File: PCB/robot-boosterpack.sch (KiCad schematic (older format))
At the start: 50 parts, among them IC1 DRV8833, IC2 TPS77033, IC3 TPS77050, IC4 LM61428, J1 3.3V Jumper, J2 5V Jumper, J3 9V Jumper, M1 MOTOR, M2 MOTOR

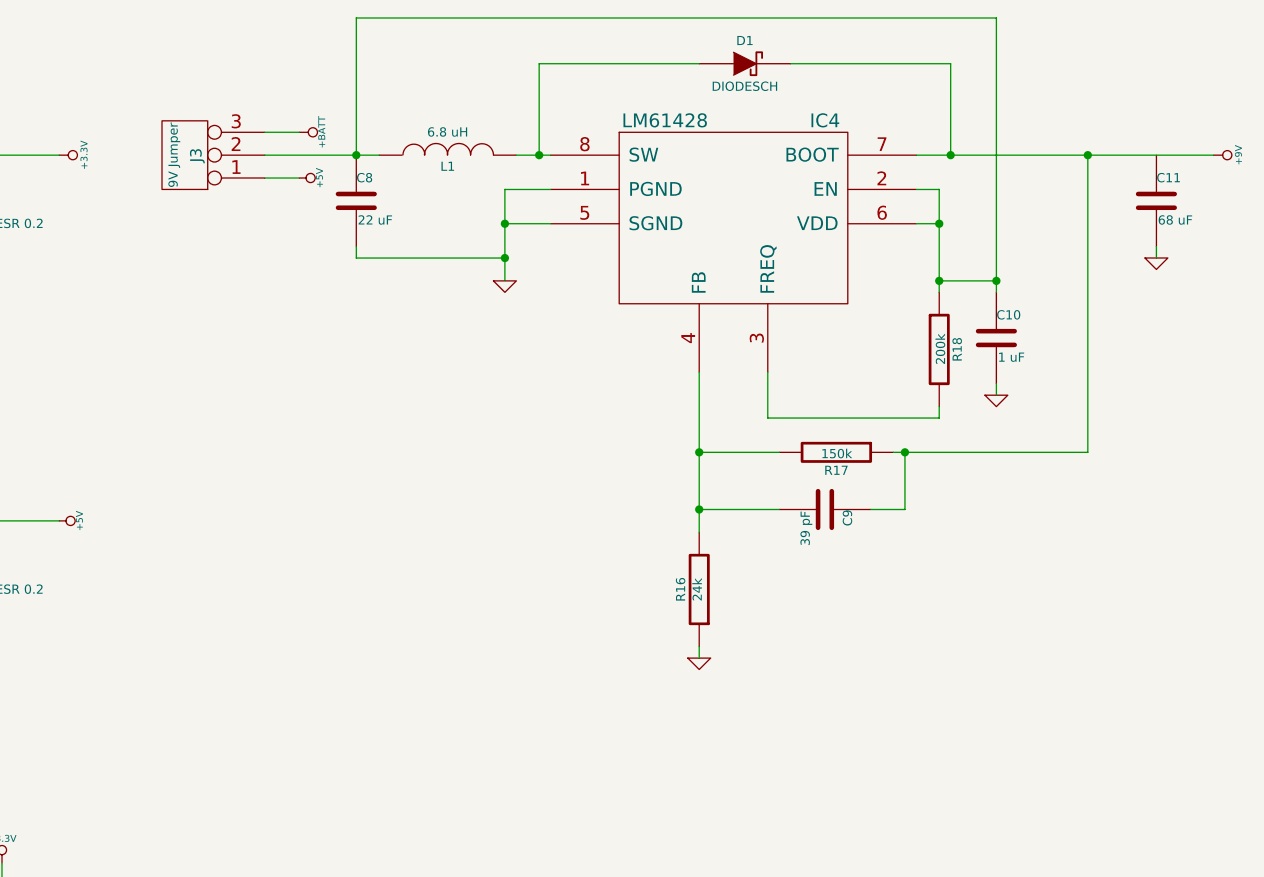
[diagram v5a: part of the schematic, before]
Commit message: added damping resistor to regulator circuit
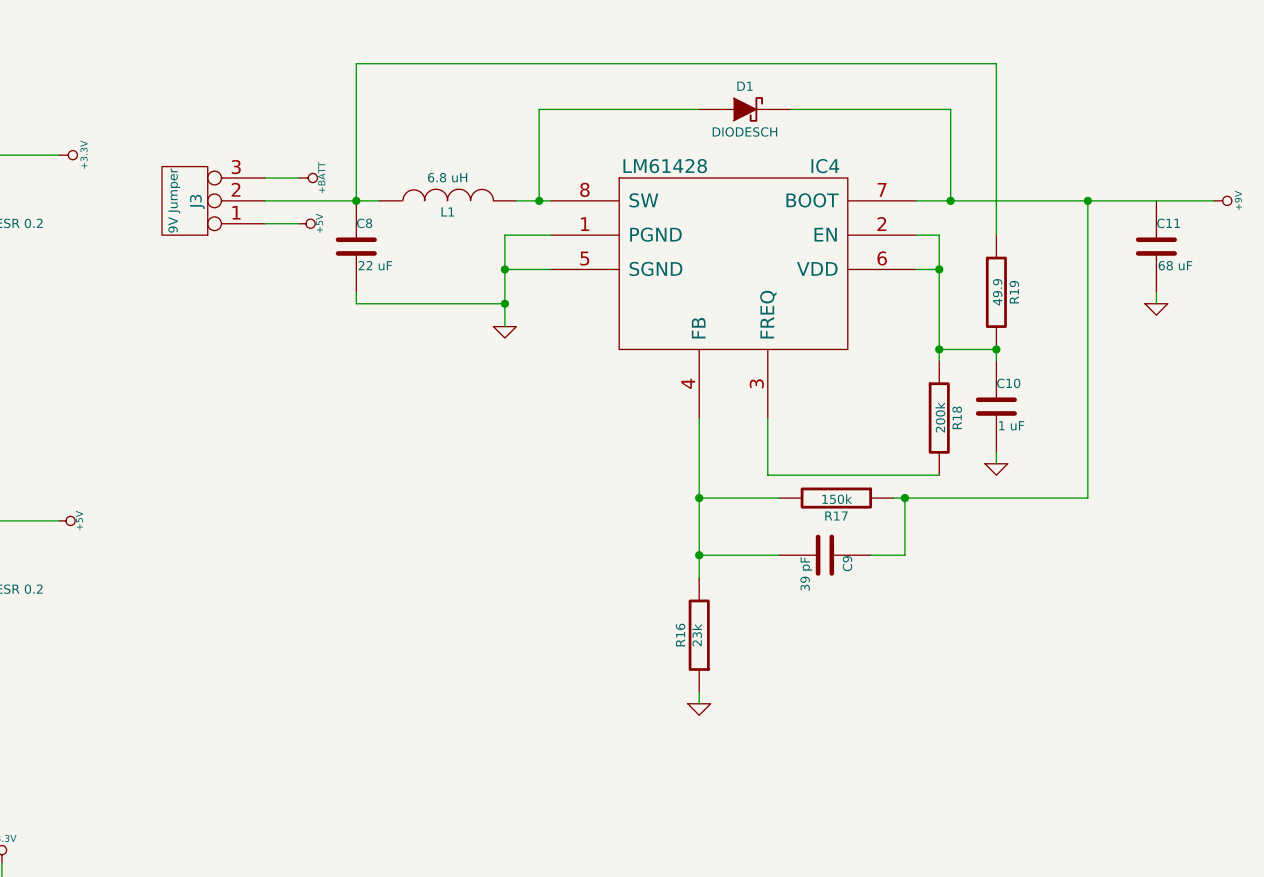
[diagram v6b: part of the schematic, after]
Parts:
- added R19: 49.9, ~, symbol R
- R16: value 24k -> 23k
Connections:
- net at C10.1, IC4.2 (EN), IC4.6 (VDD)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: now also R19.2; no longer C8.1, J3.2 (PM), L1.1
- new net: C8.1, J3.2 (PM), L1.1, R19.1
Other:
- moved on the sheet: C10, C11, C8, C9, D1, IC4, J3, L1, R16, R17, R18

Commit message: generated netlist
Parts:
- removed C11: 68 uF, ~, symbol C
- removed C8: 22 uF, ~, symbol C
- added C11: 68uF, symbol CP
- added C8: 22uF, symbol CP
- C1: Digikey # (none) -> 311-1343-1-ND
- C10: Digikey # (none) -> 587-1242-1-ND
- C2: value 2.2uF 6.3V -> 2.2 uF 6.3V; Digikey # (none) -> 587-1254-1-ND
- C3: value 1uF -> 1 uF; Digikey # (none) -> 587-1242-1-ND
- C4: Digikey # (none) -> 587-1254-1-ND
- C5: Digikey # (none) -> 490-1512-1-ND
- C6, C7: value 4.7uF ESR 0.2 -> 4.7 uF ESR 0.2; Digikey # (none) -> 478-1772-1-ND
- CONN1, J3: Digikey # (none) -> 609-3461-ND
- D1: Digikey # (none) -> MBRS140T3GOSCT-ND
- IC4: value LM61428 -> LMR61428
- J1, J2: Digikey # (none) -> 3M9447-ND
- L1: Digikey # (none) -> SRN6045-100MCT-ND
- R1, R12, R14, R6, R8: Digikey # (none) -> 311-100HRCT-ND
- R10, R2, R5, R9: Digikey # (none) -> P22KDBTR-ND
- R11, R13, R15, R4, R7: Digikey # (none) -> 311-10KGRCT-ND
- R16: value 23k -> 23.2k; Digikey # (none) -> 311-23.2KHRTR-ND
- R17: Digikey # (none) -> P150KDBCT-ND
- R18: Digikey # (none) -> P200KDBCT-ND
- R19: Digikey # (none) -> P49.9HCT-ND
- R3: Digikey # (none) -> 311-43.0KHRCT-ND
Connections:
- net +9V: now also C11.1
- net GND: now also C11.2, C8.2
- net at J3.2 (PM), L1.1, R19.1: now also C8.1

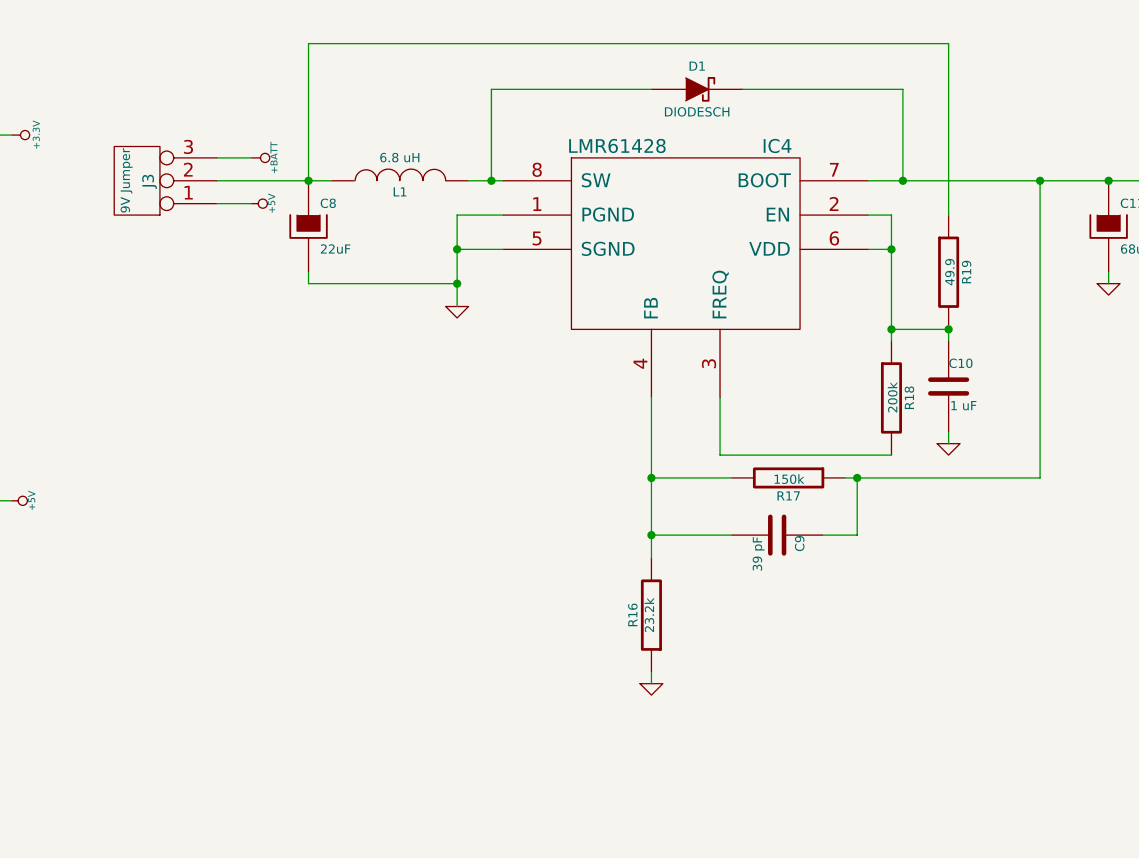
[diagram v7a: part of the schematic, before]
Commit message: added regulator status LEDs
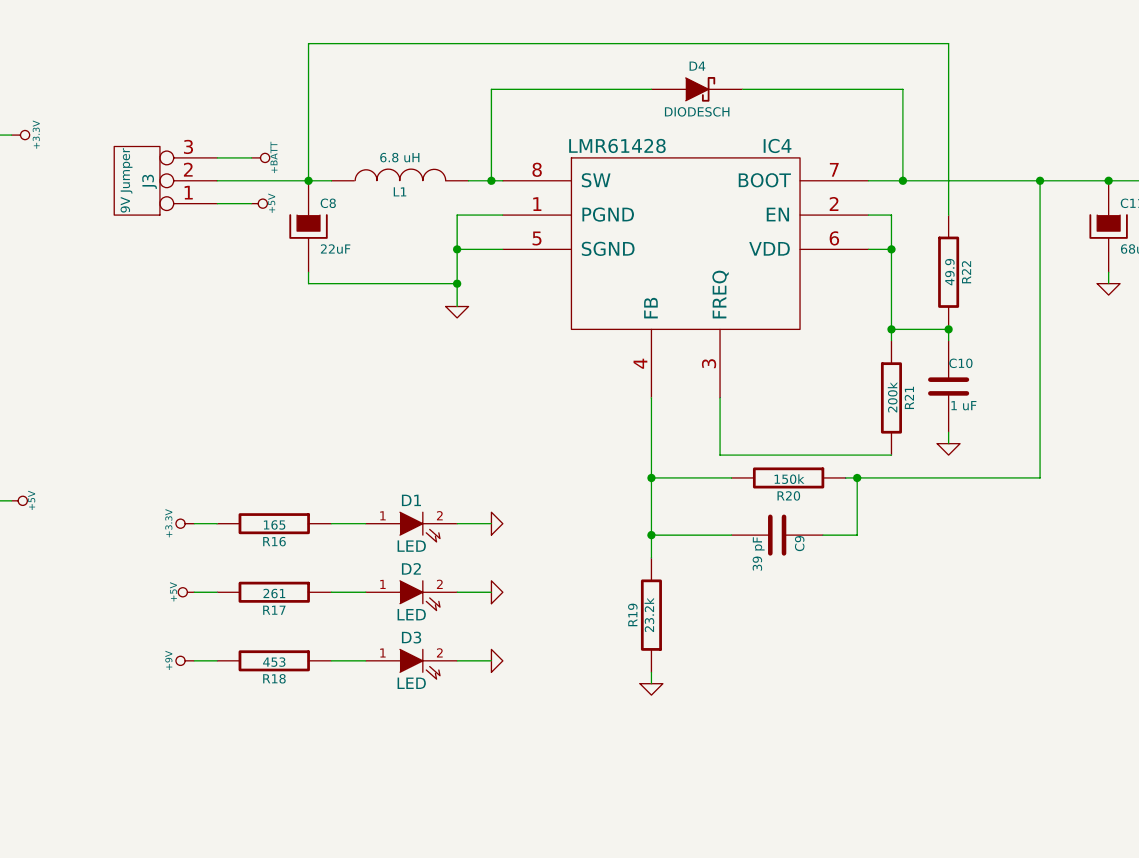
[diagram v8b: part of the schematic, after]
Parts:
- added D1, D2, D3: LED, ~, symbol LED
- added R16: 165, ~, symbol R
- added R17: 261, ~, symbol R
- added R18: 453, ~, symbol R
- renumbered D1 to D4, R16 to R19, R17 to R20, R18 to R21, R19 to R22
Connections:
- net +3.3V: now also R16.2
- net +5V: now also R17.2
- net +9V: now also R18.2
- net GND: now also D1.2 (K), D2.2 (K), D3.2 (K)
- new net: D1.1 (A), R16.1
- new net: D2.1 (A), R17.1
- new net: D3.1 (A), R18.1
